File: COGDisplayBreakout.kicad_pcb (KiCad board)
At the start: 2 copper layers, 29.2 x 31.8 mm, 14 parts, among them J1 FPC_12pin, J2 SPI_Header, J4 Conn_01x01, J5 Conn_01x01

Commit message: 3rd Rev send to OshPark
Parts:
- added C4: 1uF, Capacitor_SMD:C_0805_2012Metric, B.Cu at (137.0, 94.5)
- C1: value 1uF -> 10uF
- J1: footprint Connector_FFC-FPC:Hirose_FH12-12S-0.5SH_1x12-1MP_P0.50mm_Horizontal -> Connector_FFC-FPC:FFC_SolderPads12pos_x_0.60mm_Horizontal
- J4, J5: footprint Connector_PinHeader_2.54mm:PinHeader_1x01_P2.54mm_Vertical -> Connector_PinHeader_2.54mm:PinHeader_1x01_P2.54mm_Oblong
- R1: value 15R -> 20R
- moved C1 20.8 mm to (156.0, 85.0), turned to 0 degrees
- moved C2 2.06 mm to (156.0, 87.5)
- moved R1 1.18 mm to (137.0, 98.7)
- moved J1 1.12 mm to (148.5, 93.5)
- moved C3 0.50 mm to (137.0, 90.0), turned to -90 degrees
- renumbered C3 to C2, C2 to C3
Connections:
- C1 pad 1: /V0 -> +3V3
- C1 pad 2: /XV0 -> GND
- C3 pad 2: GND -> /XV0
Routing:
- net /VG: track 0.00 -> 9.13 mm
- net GND: track 5.69 -> 10.7 mm, vias 3 -> 2
- net +3V3: track 28.8 -> 31.8 mm
- net /SCL: track 12.1 -> 14.0 mm
- net /SDA: track 13.9 -> 15.3 mm
- net /V0: track 13.6 -> 12.2 mm
- net //CS: track 9.61 -> 10.9 mm
- net //RST: track 10.5 -> 11.7 mm
- net /A0: track 11.3 -> 12.5 mm
- net /LED_A: track 7.00 -> 5.84 mm
- net /XV0: track 11.9 -> 11.3 mm

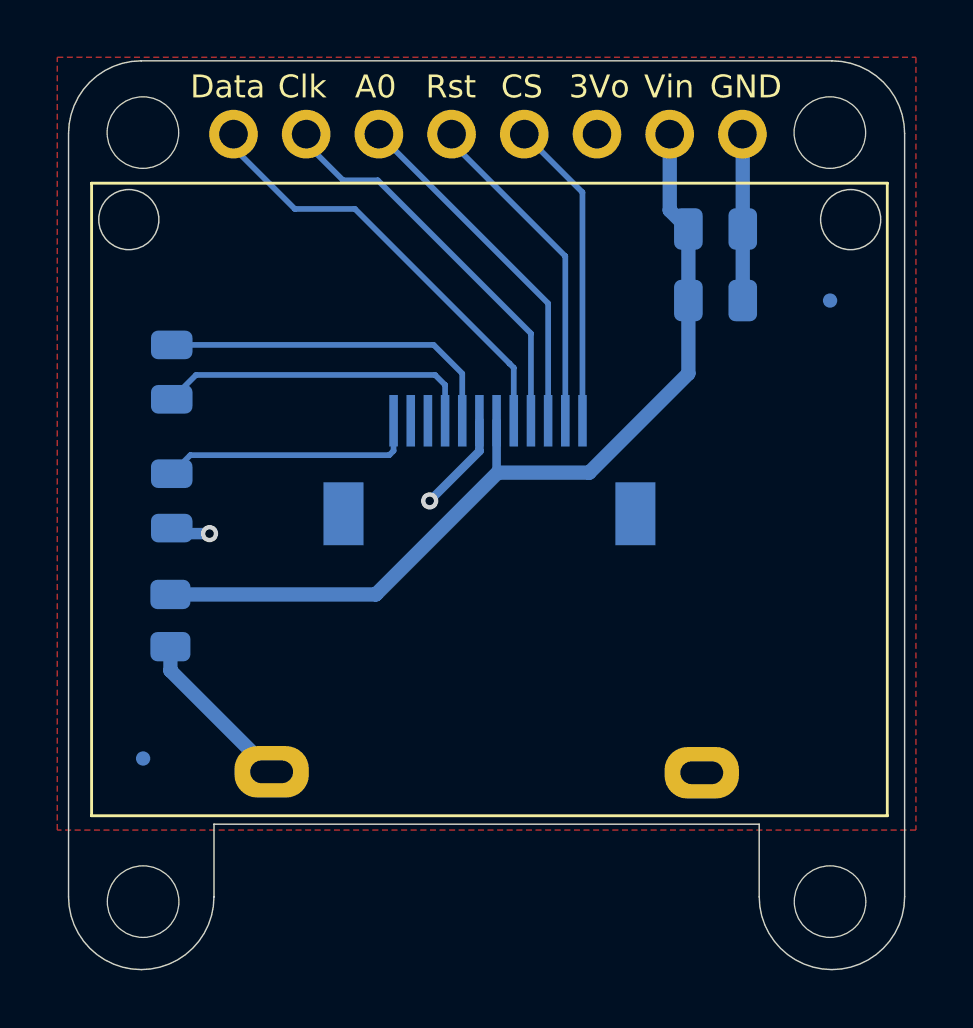
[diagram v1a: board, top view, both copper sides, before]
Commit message: Fixes v0.2 problems, new symbol and 3D model
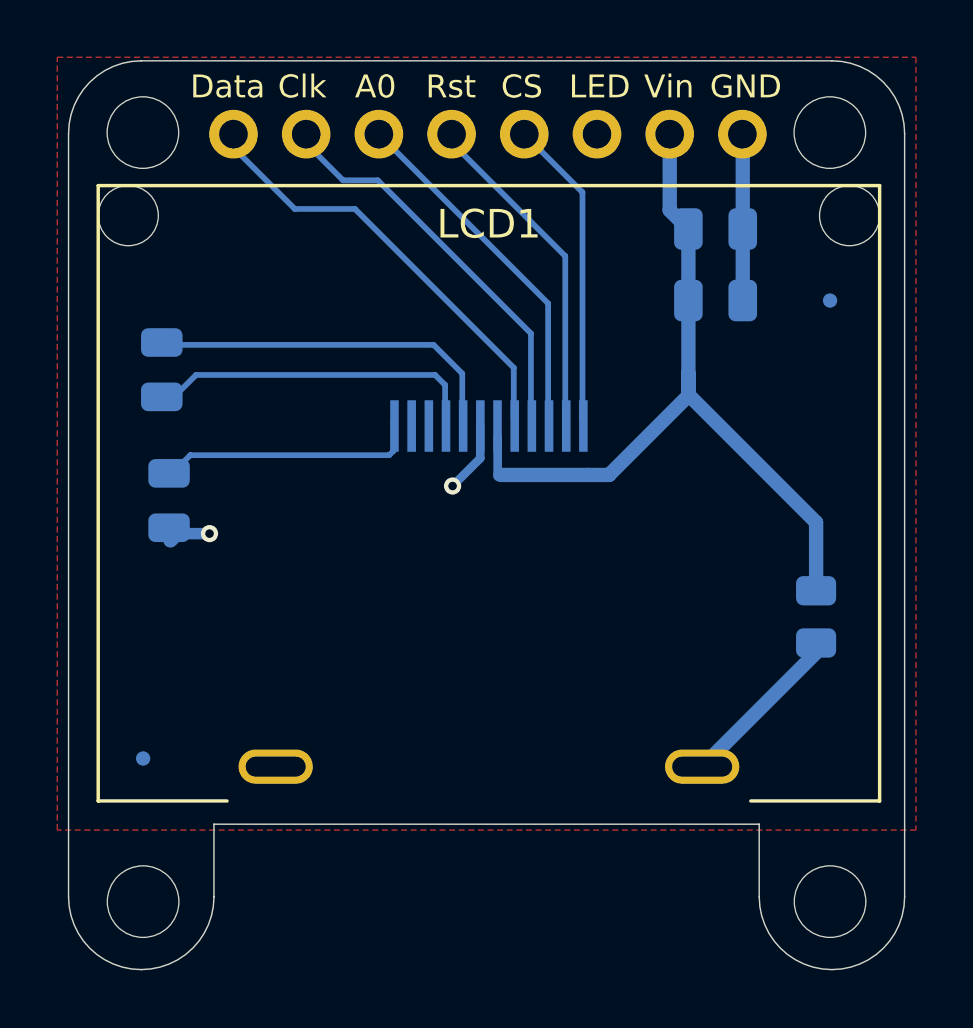
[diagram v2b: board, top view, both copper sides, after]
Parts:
- removed J1: FPC_12pin, Connector_FFC-FPC:FFC_SolderPads12pos_x_0.60mm_Horizontal
- removed J4, J5: Conn_01x01, Connector_PinHeader_2.54mm:PinHeader_1x01_P2.54mm_Oblong
- added LCD1: ERC12864FSF-11, COGDisplayBreakout:ERC12864FSF-11_COG_LCD, F.Cu at (148.1, 94.2)
- moved R1 22.6 mm to (159.5, 98.6)
- moved C3 0.36 mm to (136.7, 89.9)
- moved C4 0.09 mm to (136.9, 94.5)
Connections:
- C3 pad 1: /V0 -> Net-(LCD1-V0)
- C3 pad 2: /XV0 -> Net-(LCD1-XV0)
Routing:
- net Net-(LCD1-V0): track 0.00 -> 12.2 mm
- net /V0: track 12.2 -> 0.00 mm
- net Net-(LCD1-XV0): track 0.00 -> 11.3 mm
- net /XV0: track 11.3 -> 0.00 mm
- net +3V3: track 31.8 -> 28.0 mm
- net GND: track 10.7 -> 10.1 mm
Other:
- outline, holes or cut-outs redrawn
- board text added: "LED"
- board text removed: "3Vo"

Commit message: Rewired LED: fix A/K swap and adds control from pin 6
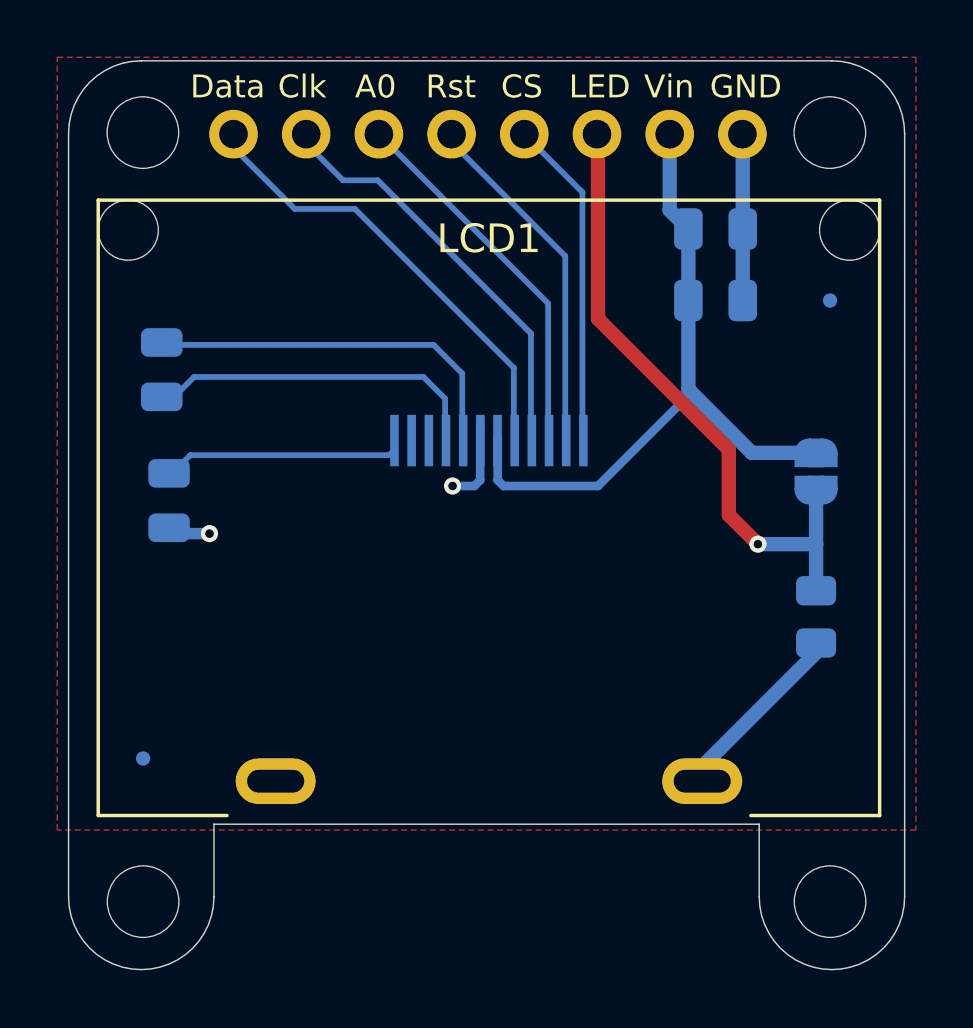
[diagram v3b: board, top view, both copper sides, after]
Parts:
- added JP1: SolderJumper_2_Open, Jumper:SolderJumper-2_P1.3mm_Open_RoundedPad1.0x1.5mm, B.Cu at (159.5, 93.5)
- moved LCD1 0.51 mm to (148.1, 94.7)
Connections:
- J2 pad 6: unconnected-(J2-Pin_6-Pad6) -> /LED
- R1 pad 1: +3V3 -> /LED
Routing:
- net /LED: track 0.00 -> 22.2 mm, vias 0 -> 1
- net +3V3: track 28.0 -> 24.1 mm
- net /VG: track 9.13 -> 8.08 mm

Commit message: Ensure Handsolder 0805 footprints
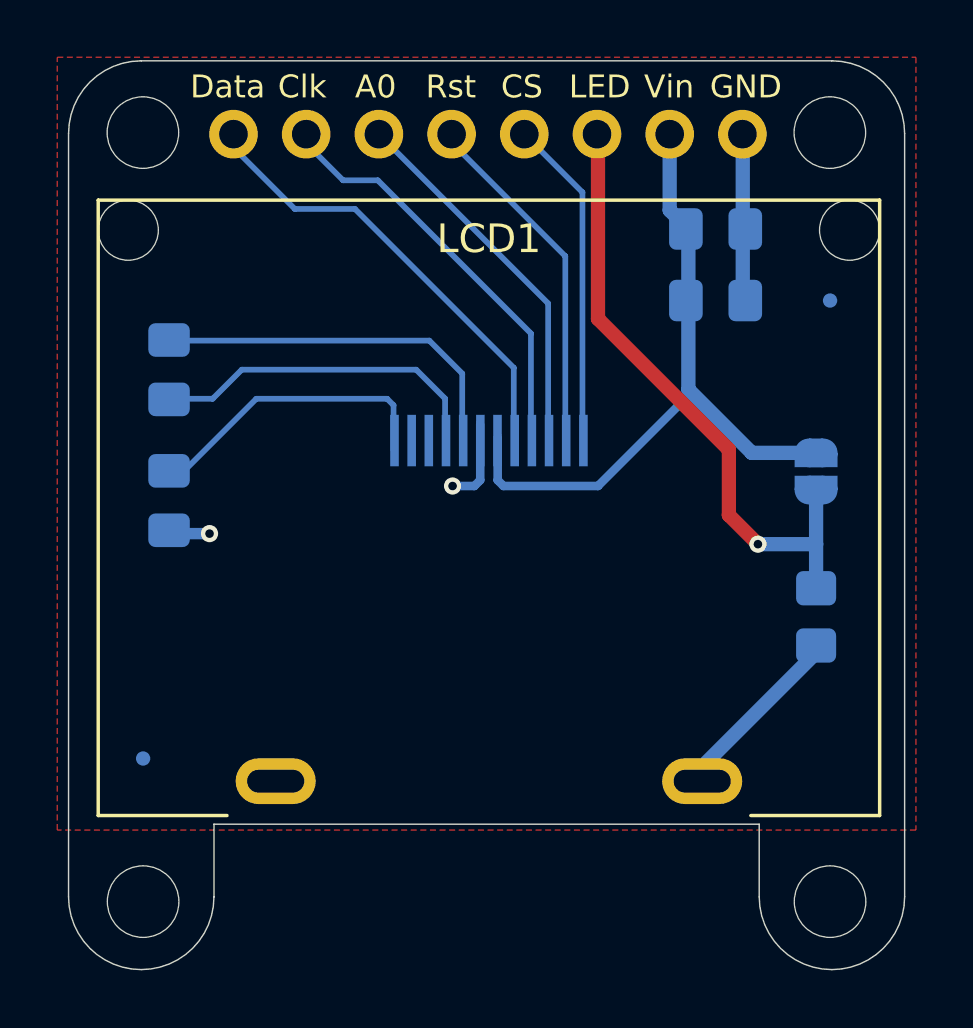
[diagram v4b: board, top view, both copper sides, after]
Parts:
- C1, C2, C3, C4: footprint Capacitor_SMD:C_0805_2012Metric -> Capacitor_SMD:C_0805_2012Metric_Pad1.18x1.45mm_HandSolder
- R1: footprint Resistor_SMD:R_0805_2012Metric -> Resistor_SMD:R_0805_2012Metric_Pad1.20x1.40mm_HandSolder
- moved C3 0.25 mm to (136.9, 89.9)
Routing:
- net /VG: track 8.08 -> 10.5 mm

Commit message: readme edits
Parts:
- renumbered J2 to J1
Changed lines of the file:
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@@
 		(descr "Through hole straight pin header, 1x08, 2.54mm pitch, single row")
 		(tags "Through hole pin header THT 1x08 2.54mm single row")
-		(property "Reference" "J2"
+		(property "Reference" "J1"
 			(at 0 2.38 90)
 			(layer "B.SilkS")

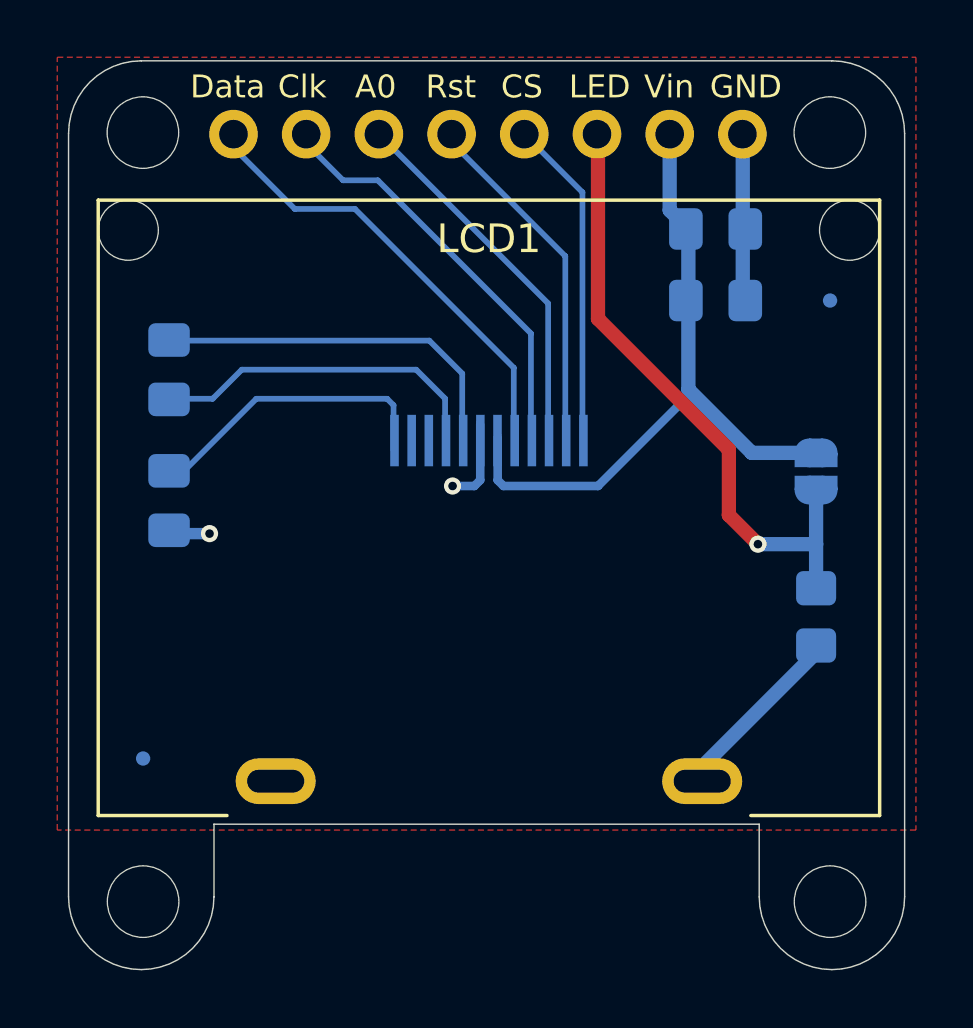
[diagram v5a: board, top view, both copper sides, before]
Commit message: Adds power on reset
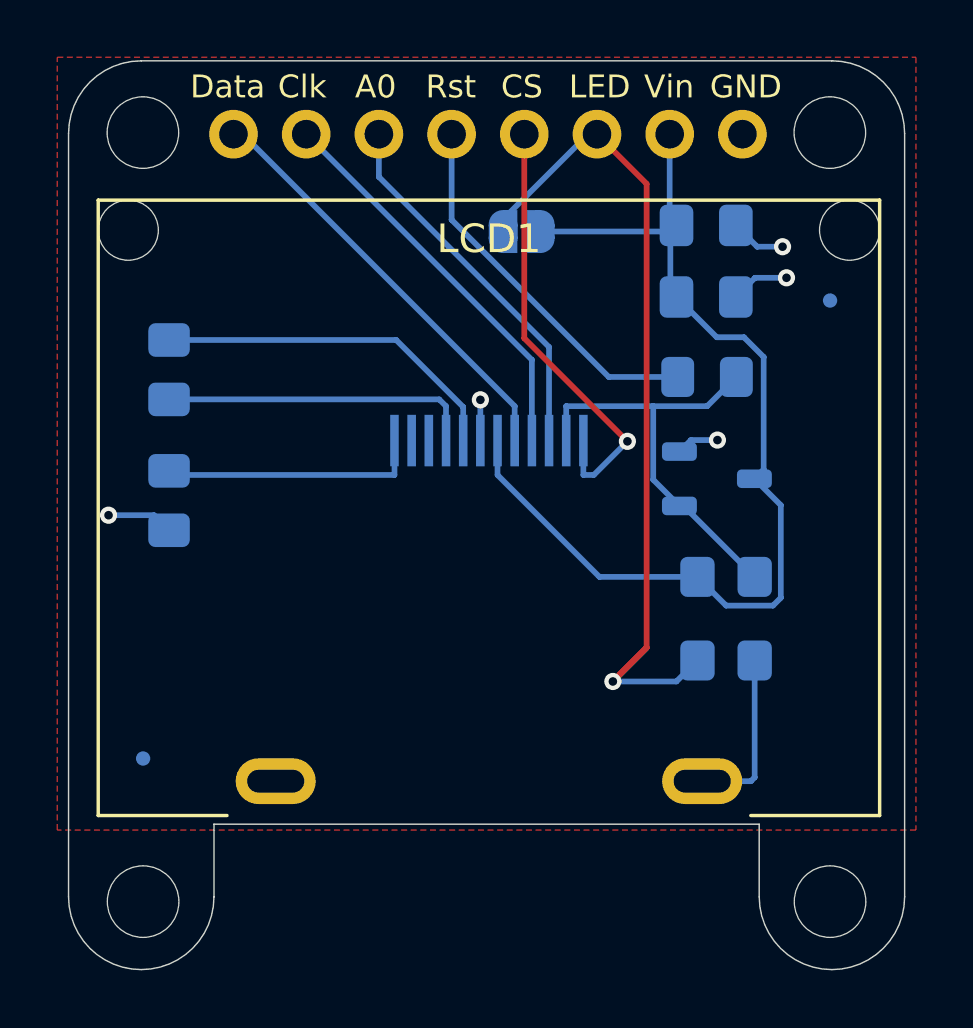
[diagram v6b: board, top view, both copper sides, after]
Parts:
- added D1: 1N4148, Diode_SMD:D_0805_2012Metric_Pad1.15x1.40mm_HandSolder, B.Cu at (155.7, 90.2)
- added R2: R, Resistor_SMD:R_0805_2012Metric_Pad1.20x1.40mm_HandSolder, B.Cu at (156.4, 97.2)
- added U1: APX803S, Package_TO_SOT_SMD:TSOT-23, B.Cu at (156.0, 93.7)
- moved JP1 13.3 mm to (149.2, 85.1), turned to 0 degrees
- moved R1 3.49 mm to (156.4, 100.1), turned to 0 degrees
- moved C1 0.35 mm to (155.7, 84.9)
- moved C2 0.35 mm to (155.7, 87.4)
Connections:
- LCD1 pad 2: //RST -> //RES_3V
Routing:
- net //RES_3V: track 0.00 -> 15.1 mm
- net /LED: track 22.2 -> 35.2 mm
- net +3V3: track 24.1 -> 36.5 mm
- net //CS: track 10.9 -> 15.4 mm, vias 0 -> 1
- net //RST: track 11.7 -> 13.2 mm
- net /VG: track 10.5 -> 9.14 mm
- net GND: track 10.2 -> 9.23 mm, vias 2 -> 5
- net /A0: track 12.5 -> 13.2 mm

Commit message: new board layout for power-on reset
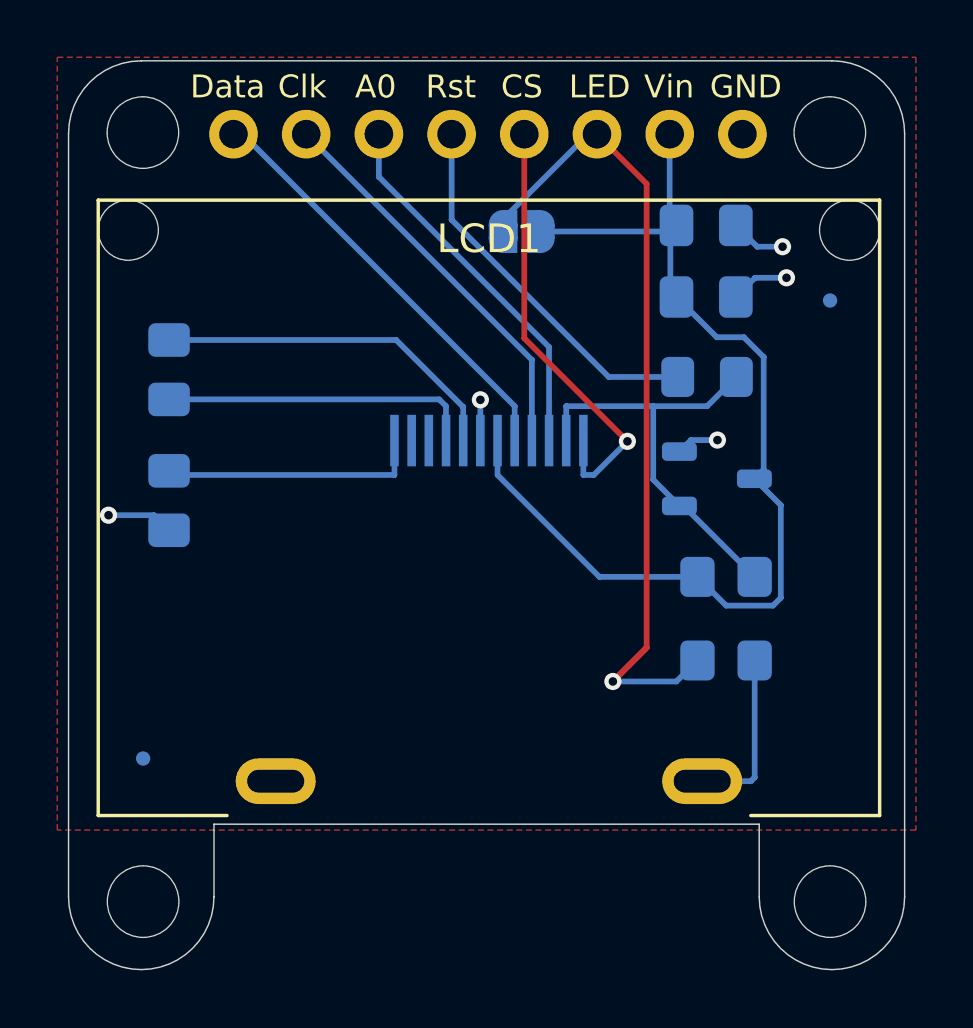
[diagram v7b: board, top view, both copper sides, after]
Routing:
- net /LED: track 35.2 -> 31.9 mm
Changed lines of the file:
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@@
 			(drillshape 0)
 			(scaleselection 1)
-			(outputdirectory "Gerbers20260403/")
+			(outputdirectory "Gerbers20260415/")
 		)
 	)
@@
 	)
 	(segment
-		(start 153.5911 99.6293)
-		(end 152.4115 100.8089)
+		(start 151.8573 81.6871)
+		(end 153.5911 83.4209)
 		(width 0.2)
 		(layer "F.Cu")
@@
 	)
 	(segment
-		(start 151.8573 81.6871)
-		(end 153.5911 83.4209)
+		(start 153.5911 99.6293)
+		(end 152.4115 100.8089)
 		(width 0.2)
 		(layer "F.Cu")
@@
 	)
 	(segment
-		(start 153.5911 99.6293)
-		(end 152.4115 100.8089)
-		(width 0.2)
-		(layer "B.Cu")
-		(net 14)
-	)
-	(segment
 		(start 151.5511 81.6871)
 		(end 148.575 84.6632)
 		(width 0.2)
 		(layer "B.Cu")
-		(net 14)
-	)
-	(segment
-		(start 152.4115 100.8089)
-		(end 153.5911 99.6293)
-		(width 0.2)
-		(layer "B.Cu")
